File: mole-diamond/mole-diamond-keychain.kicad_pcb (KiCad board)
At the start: 2 copper layers, 50.8 x 57.2 mm, 7 parts

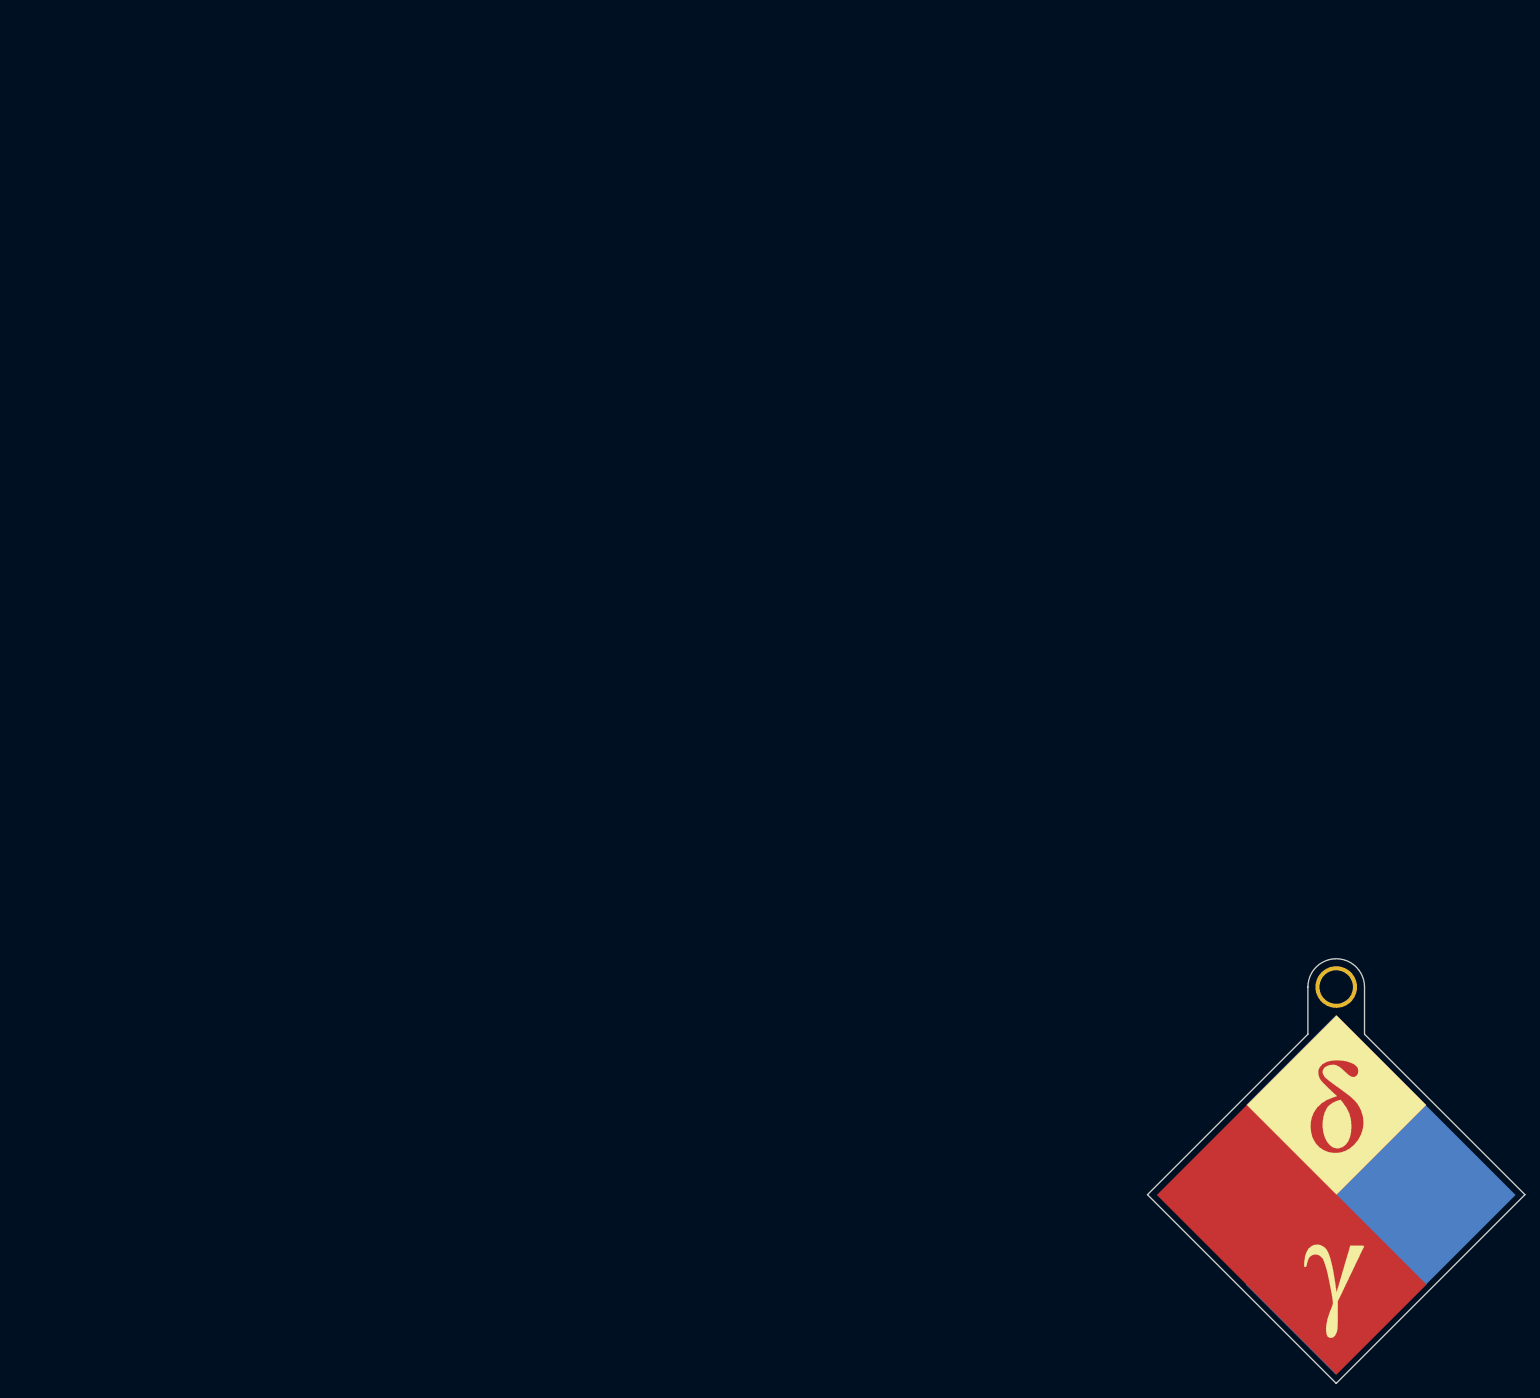
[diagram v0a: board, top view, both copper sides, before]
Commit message: Locate bottom corner at absolute origin
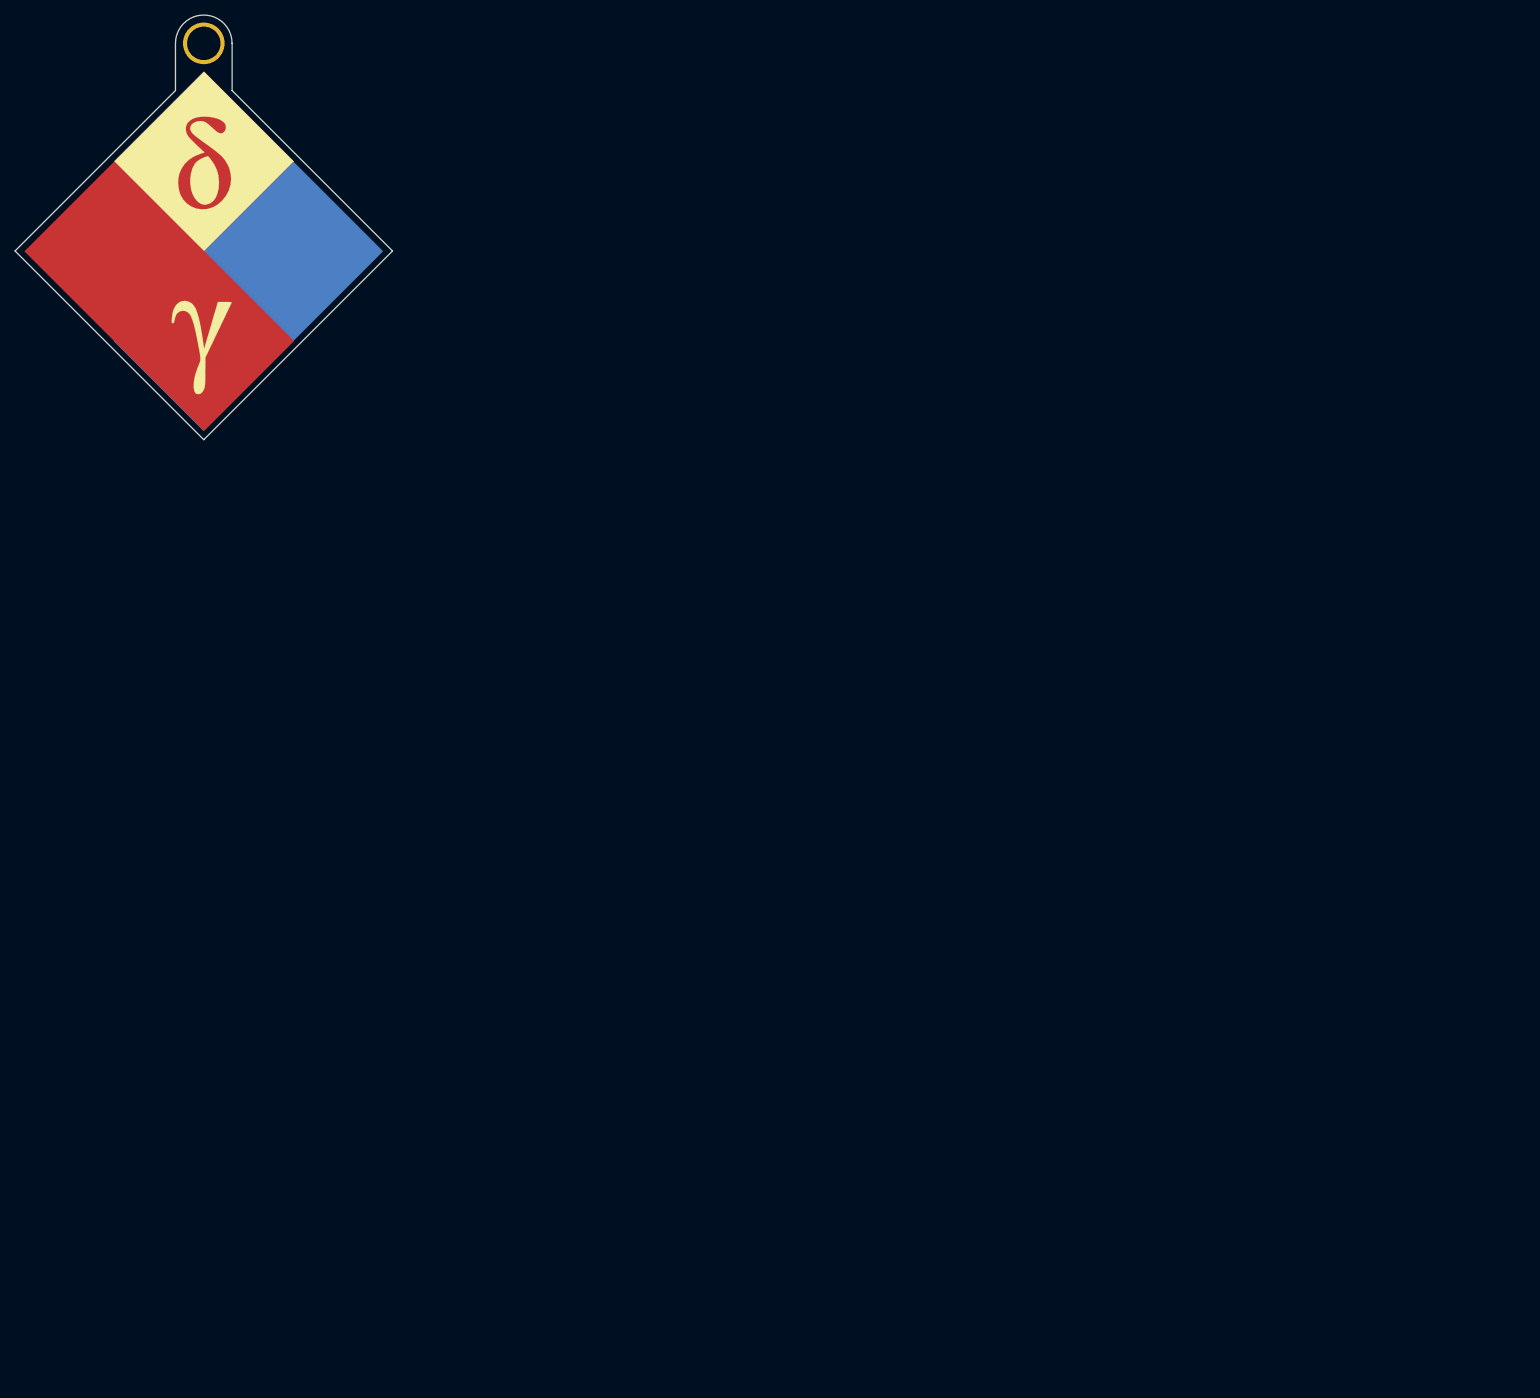
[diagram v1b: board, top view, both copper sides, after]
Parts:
- moved G*** 198.4 mm to (0.00, -25.4) (x6)
- moved REF** 198.4 mm to (0.00, -53.3)
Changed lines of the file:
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@@
     (solder_mask_min_width 0.25)
     (aux_axis_origin 0 0)
-    (grid_origin 127 127)
-    (visible_elements FFFFFF7F)
+    (visible_elements 7FFFFFFF)
     (pcbplotparams
-      (layerselection 0x010fc_ffffffff)
+      (layerselection 0x010f0_ffffffff)
       (usegerberextensions false)
       (usegerberattributes false)
@@
       (outputformat 1)
       (mirror false)
-      (drillshape 1)
+      (drillshape 0)
       (scaleselection 1)
-      (outputdirectory ""))
+      (outputdirectory "gerber/"))
   )
   (net 0 "")
@@
   )
   (module crest:blacker_diamond_300_cu (layer B.Cu)
-    (at 152.4 101.6 180)
+    (at 0 -25.4 180)
     (fp_text reference G*** (at 0 0) (layer B.SilkS) hide
       (effects (font (size 1.524 1.524) (thickness 0.3)) (justify mirror))
@@
   )
   (module crest:blacker_diamond_300_cu (layer F.Cu)
-    (at 152.4 101.6)
+    (at 0 -25.4)
     (fp_text reference G*** (at 0 0) (layer F.SilkS) hide
       (effects (font (size 1.524 1.524) (thickness 0.3)))
@@
   )
   (module crest:blacker_diamond_300_silk (layer B.Cu)
-    (at 152.4 101.6 180)
+    (at 0 -25.4 180)
     (fp_text reference G*** (at 0 0) (layer B.SilkS) hide
       (effects (font (size 1.524 1.524) (thickness 0.3)) (justify mirror))
@@
   )
   (module crest:blacker_diamond_300_silk (layer F.Cu)
-    (at 152.4 101.6)
+    (at 0 -25.4)
     (fp_text reference G*** (at 0 0) (layer F.SilkS) hide
       (effects (font (size 1.524 1.524) (thickness 0.3)))
@@
   )
   (module crest:blacker_diamond_300_mask (layer B.Cu)
-    (at 152.4 101.6 180)
+    (at 0 -25.4 180)
     (fp_text reference G*** (at 0 0) (layer B.SilkS) hide
       (effects (font (size 1.524 1.524) (thickness 0.3)) (justify mirror))
@@
   )
   (module crest:blacker_diamond_300_mask (layer F.Cu)
-    (at 152.4 101.6)
+    (at 0 -25.4)
     (fp_text reference G*** (at 0 0) (layer F.SilkS) hide
       (effects (font (size 1.524 1.524) (thickness 0.3)))
@@
   )
   (module MountingHole:MountingHole_4.5mm_Pad (layer F.Cu)
-    (at 152.4 73.66)
+    (at 0 -53.34)
     (descr "Mounting Hole 4.5mm")
     (tags "mounting hole 4.5mm")
@@
   )
   (dimension 5.08 (width 0.15) (layer Dwgs.User)
-    (gr_text "5.080 mm" (at 149.86 62.2) (layer Dwgs.User)
+    (gr_text "5.080 mm" (at -2.54 -64.8) (layer Dwgs.User)
       (effects (font (size 1 1) (thickness 0.15)))
     )
-    (feature1 (pts (xy 152.4 66.04) (xy 152.4 62.913579)))
-    (feature2 (pts (xy 147.32 66.04) (xy 147.32 62.913579)))
-    (crossbar (pts (xy 147.32 63.5) (xy 152.4 63.5)))
-    (arrow1a (pts (xy 152.4 63.5) (xy 151.273496 64.086421)))
-    (arrow1b (pts (xy 152.4 63.5) (xy 151.273496 62.913579)))
-    (arrow2a (pts (xy 147.32 63.5) (xy 148.446504 64.086421)))
-    (arrow2b (pts (xy 147.32 63.5) (xy 148.446504 62.913579)))
-  )
-  (gr_line (start 127 124.46) (end 127 66.04) (layer Dwgs.User) (width 0.15))
-  (gr_line (start 129.54 127) (end 180.34 127) (layer Dwgs.User) (width 0.15))
-  (gr_arc (start 152.4 73.66) (end 156.21 73.66) (angle -180) (layer Edge.Cuts) (width 0.05))
-  (gr_line (start 156.21 80.01) (end 156.21 73.66) (layer Edge.Cuts) (width 0.05))
-  (gr_line (start 148.59 73.66) (end 148.59 80.01) (layer Edge.Cuts) (width 0.05))
-  (gr_line (start 177.8 101.6) (end 152.4 127) (layer Edge.Cuts) (width 0.05))
-  (gr_line (start 156.21 80.01) (end 177.8 101.6) (layer Edge.Cuts) (width 0.05))
-  (gr_line (start 127 101.6) (end 148.59 80.01) (layer Edge.Cuts) (width 0.05))
-  (gr_line (start 152.4 127) (end 127 101.6) (layer Edge.Cuts) (width 0.05))
+    (feature1 (pts (xy 0 -60.96) (xy 0 -64.086421)))
+    (feature2 (pts (xy -5.08 -60.96) (xy -5.08 -64.086421)))
+    (crossbar (pts (xy -5.08 -63.5) (xy 0 -63.5)))
+    (arrow1a (pts (xy 0 -63.5) (xy -1.126504 -62.913579)))
+    (arrow1b (pts (xy 0 -63.5) (xy -1.126504 -64.086421)))
+    (arrow2a (pts (xy -5.08 -63.5) (xy -3.953496 -62.913579)))
+    (arrow2b (pts (xy -5.08 -63.5) (xy -3.953496 -64.086421)))
+  )
+  (gr_line (start -25.4 0) (end -25.4 -60.96) (layer Dwgs.User) (width 0.15))
+  (gr_line (start -25.4 0) (end 27.94 0) (layer Dwgs.User) (width 0.15))
+  (gr_arc (start 0 -53.34) (end 3.81 -53.34) (angle -180) (layer Edge.Cuts) (width 0.05))
+  (gr_line (start 3.81 -46.99) (end 3.81 -53.34) (layer Edge.Cuts) (width 0.05))
+  (gr_line (start -3.81 -53.34) (end -3.81 -46.99) (layer Edge.Cuts) (width 0.05))
+  (gr_line (start 25.4 -25.4) (end 0 0) (layer Edge.Cuts) (width 0.05))
+  (gr_line (start 3.81 -46.99) (end 25.4 -25.4) (layer Edge.Cuts) (width 0.05))
+  (gr_line (start -25.4 -25.4) (end -3.81 -46.99) (layer Edge.Cuts) (width 0.05))
+  (gr_line (start 0 0) (end -25.4 -25.4) (layer Edge.Cuts) (width 0.05))
 )
